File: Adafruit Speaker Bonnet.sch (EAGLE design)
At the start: 29 parts, among them X1 3.5mm, X2 3.5mm, X3 4 JST-PH

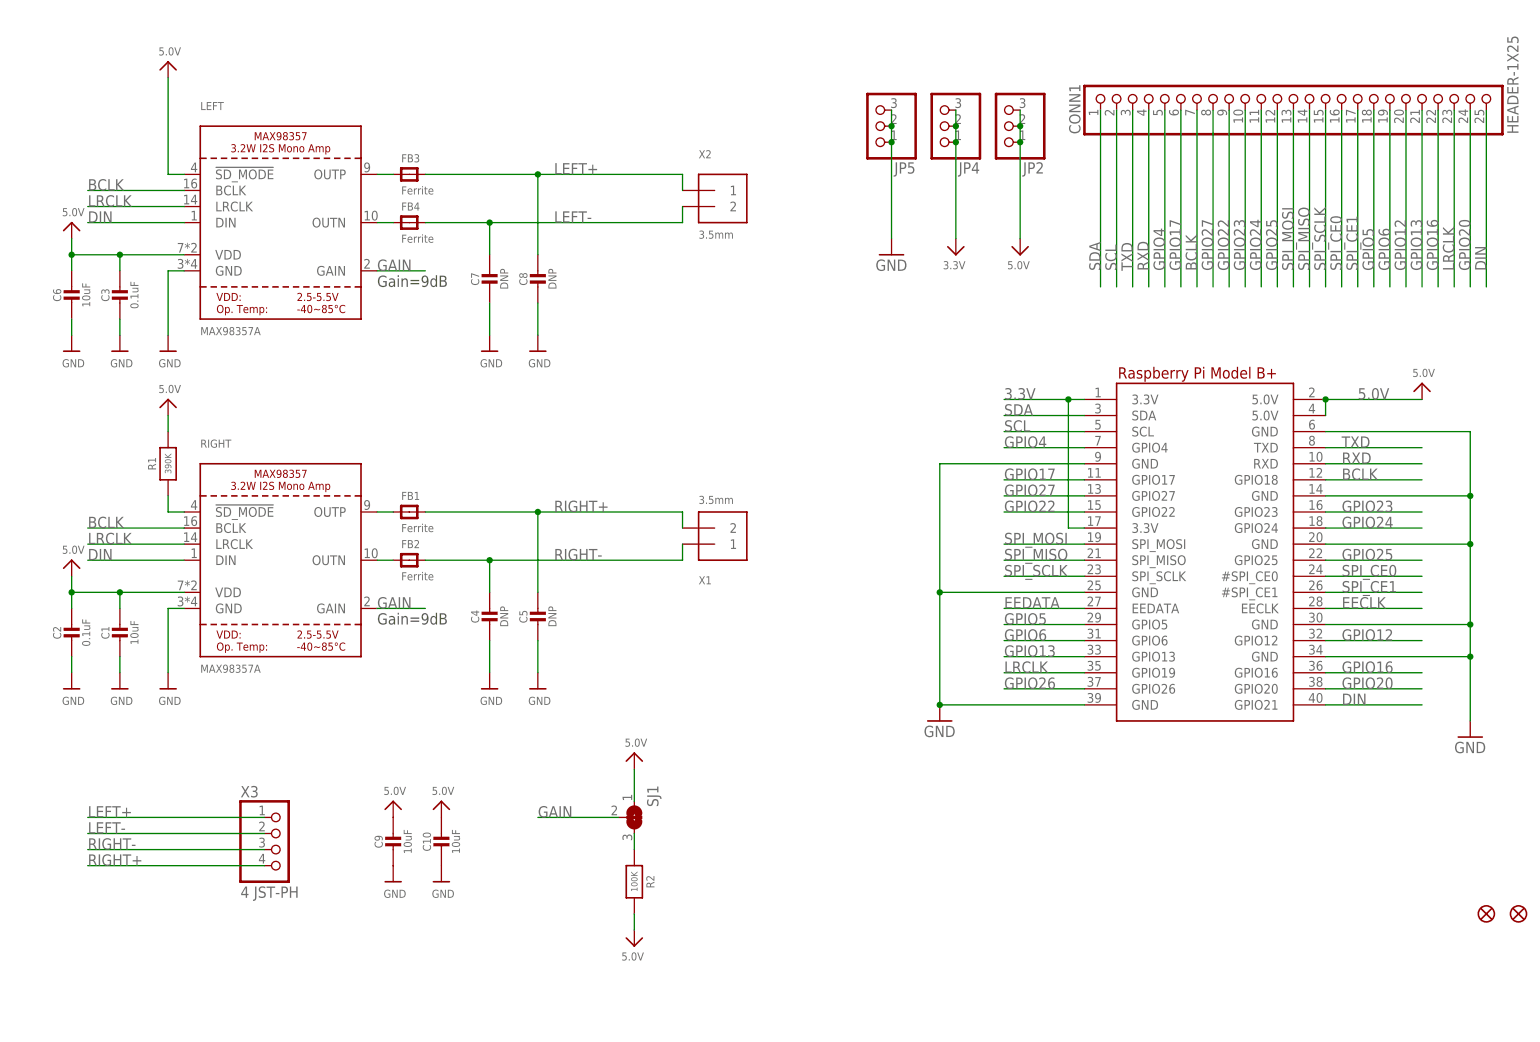
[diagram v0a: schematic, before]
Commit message: fix pop problem
MAX98357A not in shutdown when no clocks are present (no auto-detect). !SD_MODE is a multi-level comparator with an internal 100k pull-down.
* disconnect !SD_MODE pins from PU to 5V
* connect LEFT channel directly to selector
* connect RIGHT channel through R_SMALL (3.3V:220k) to selector
* selector allows selection between always-on (PU to 3.3V instead of 5V to avoid accidental GPIO bridging to 5V) and GPIO4
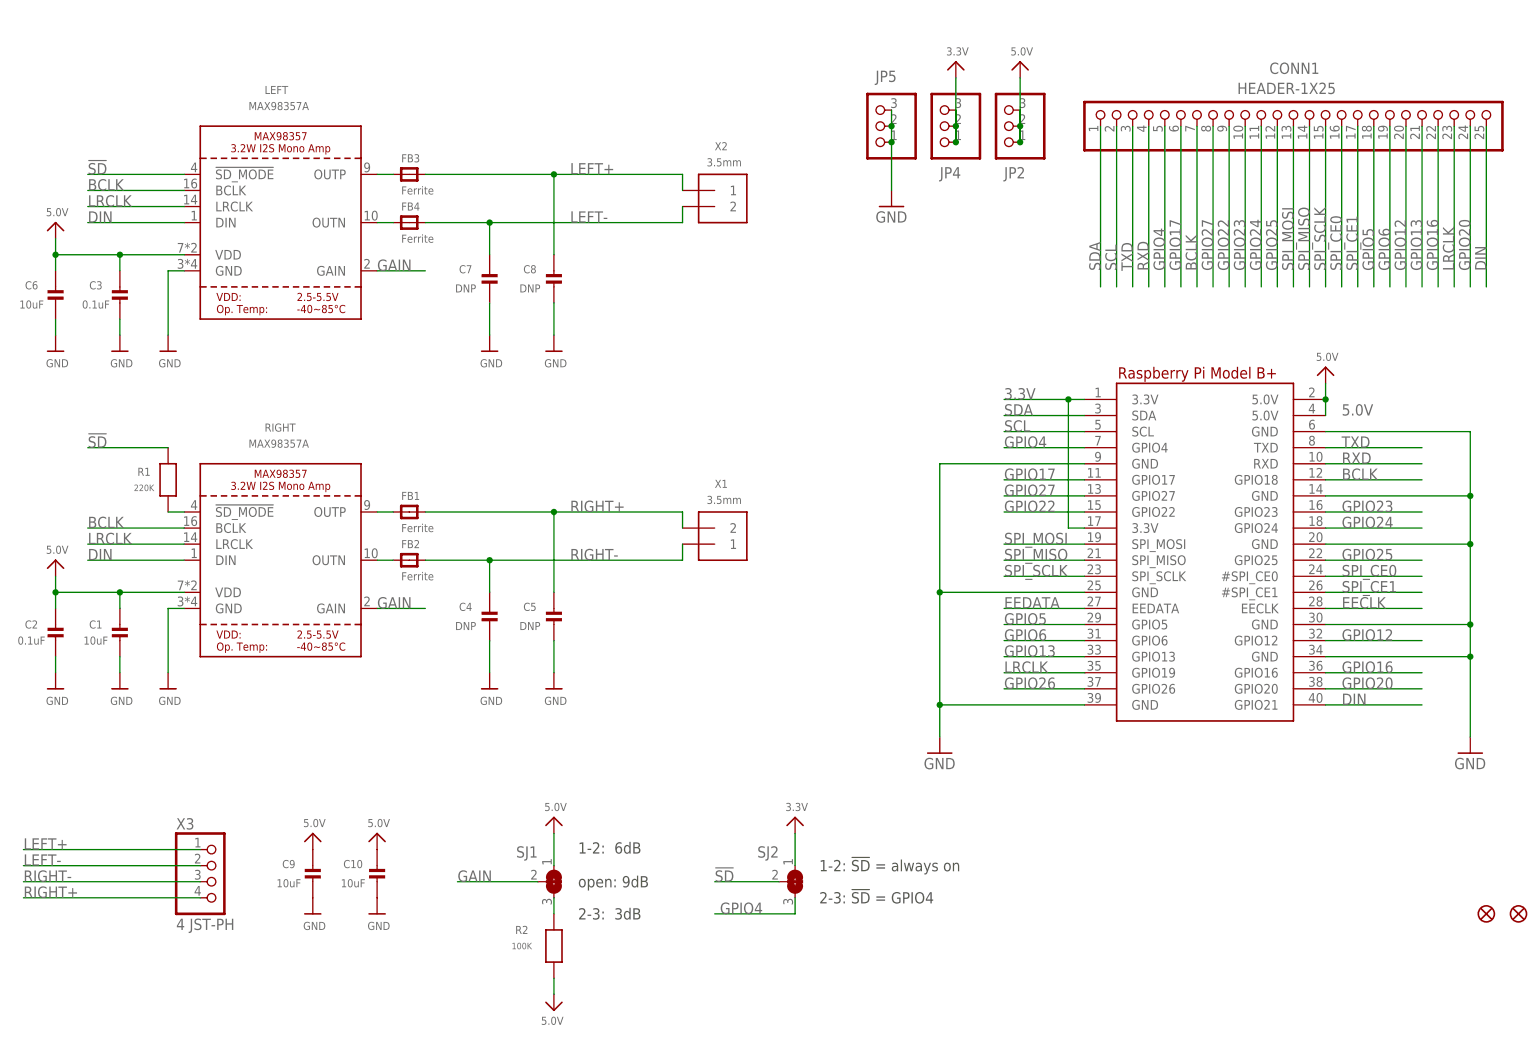
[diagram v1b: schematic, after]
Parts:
- added SJ2: (no value), microbuilder:SOLDERJUMPER_2WAY
- R1: value 390K -> 220K
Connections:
- new net !SD: LEFT.!SD_MODE, R1.2, SJ2.2
- net 3.3V: now also SJ2.1
- net 5.0V: no longer LEFT.!SD_MODE, R1.2
- net GPIO4: now also SJ2.3
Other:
- note added: "1-2: !SD! = always on"
- note added: "1-2: 6dB"
- note added: "2-3: !SD! = GPIO4"
- note added: "2-3: 3dB"
- note added: "open: 9dB"
- note removed: "Gain=9dB"
- moved on the sheet: C10, C2, C5, C6, C8, C9, CONN1, R1, R2, SJ1, X3

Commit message: swap LEFT-RIGHT
* swap channels (does not impact software side)
* upate silkscreen (now right-side output is actually RIGHT channel)
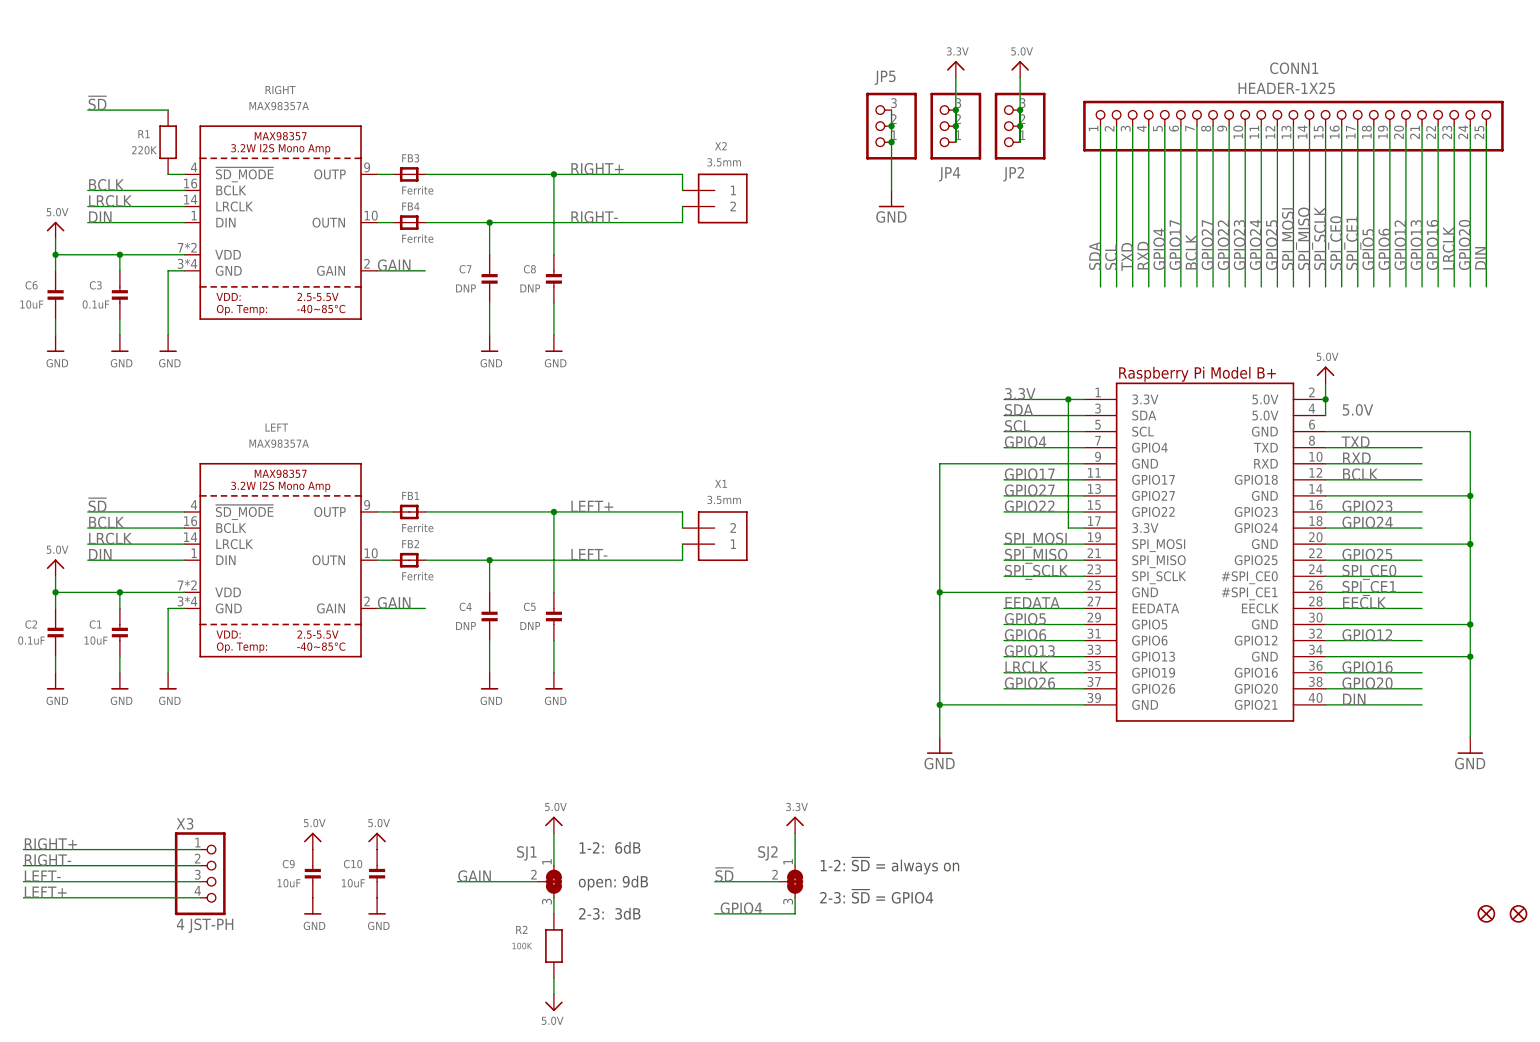
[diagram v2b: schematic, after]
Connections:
- removed net SD_MODE: R1.1, RIGHT.!SD_MODE
- new net N$3: R1.2, RIGHT.!SD_MODE
- net !SD: now also R1.1; no longer R1.2
- net LEFT+: now also C5.1, FB1.P$2, X1.2, X3.4; no longer C8.1, FB3.P$2, X2.1, X3.1
- net LEFT-: now also C4.1, FB2.P$2, X1.1, X3.3; no longer C7.1, FB4.P$2, X2.2, X3.2
- net N$1: now also RIGHT.OUTN; no longer LEFT.OUTN
- net N$2: now also RIGHT.OUTP; no longer LEFT.OUTP
- net N$5: now also LEFT.OUTN; no longer RIGHT.OUTN
- net N$6: now also LEFT.OUTP; no longer RIGHT.OUTP
- net RIGHT+: now also C8.1, FB3.P$2, X2.1, X3.1; no longer C5.1, FB1.P$2, X1.2, X3.4
- net RIGHT-: now also C7.1, FB4.P$2, X2.2, X3.2; no longer C4.1, FB2.P$2, X1.1, X3.3
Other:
- moved on the sheet: LEFT, R1, RIGHT
